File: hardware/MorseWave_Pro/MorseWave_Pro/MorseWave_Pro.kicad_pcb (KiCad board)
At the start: 2 copper layers, 85 x 65 mm, 33 parts, among them J1 PADDLE_3.5mm, J2 KEY_OUT_3.5mm, J3 PTT_OUT_RCA, J4 SPEAKER_8R, J5 OLED_0.96_I2C, J6 PS2_KEYBOARD, Q1 BC547, U2 PC817, U3 PC817

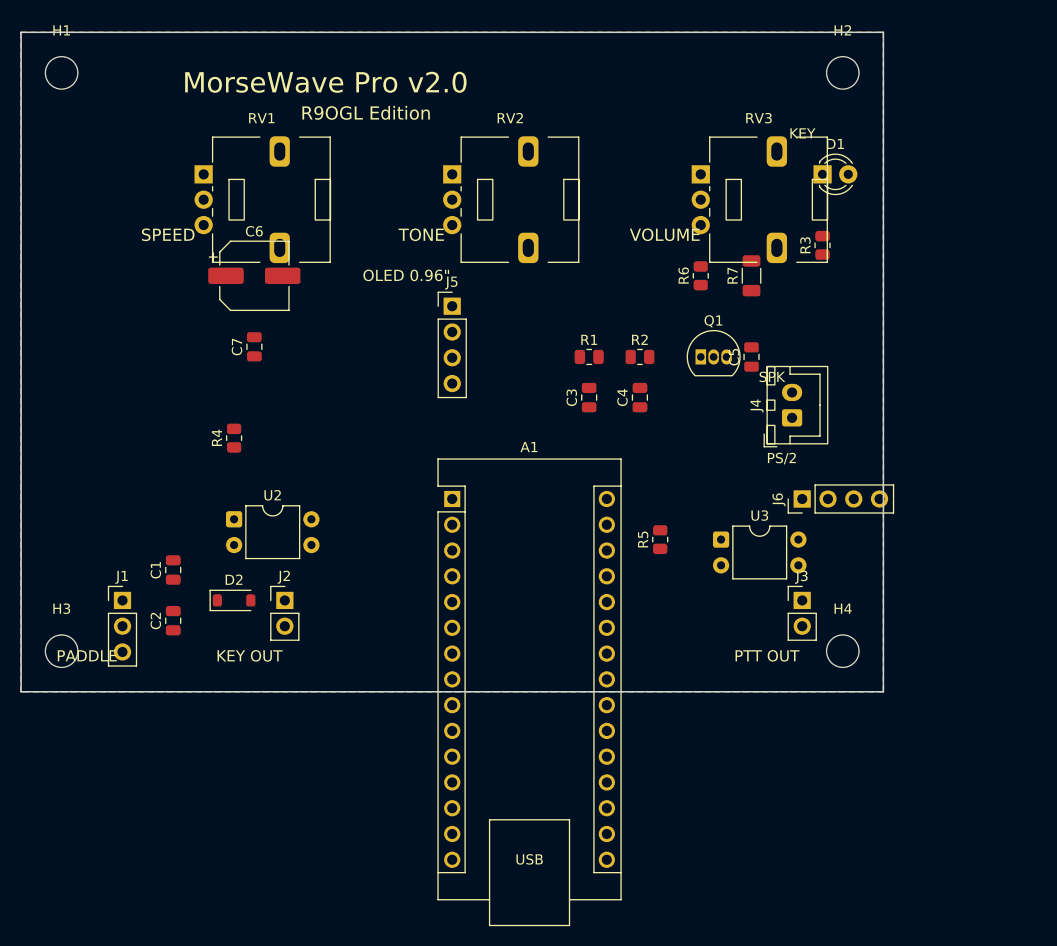
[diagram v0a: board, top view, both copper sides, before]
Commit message: Resize board to 100x75mm so Arduino Nano fits 100% inside with flush USB port
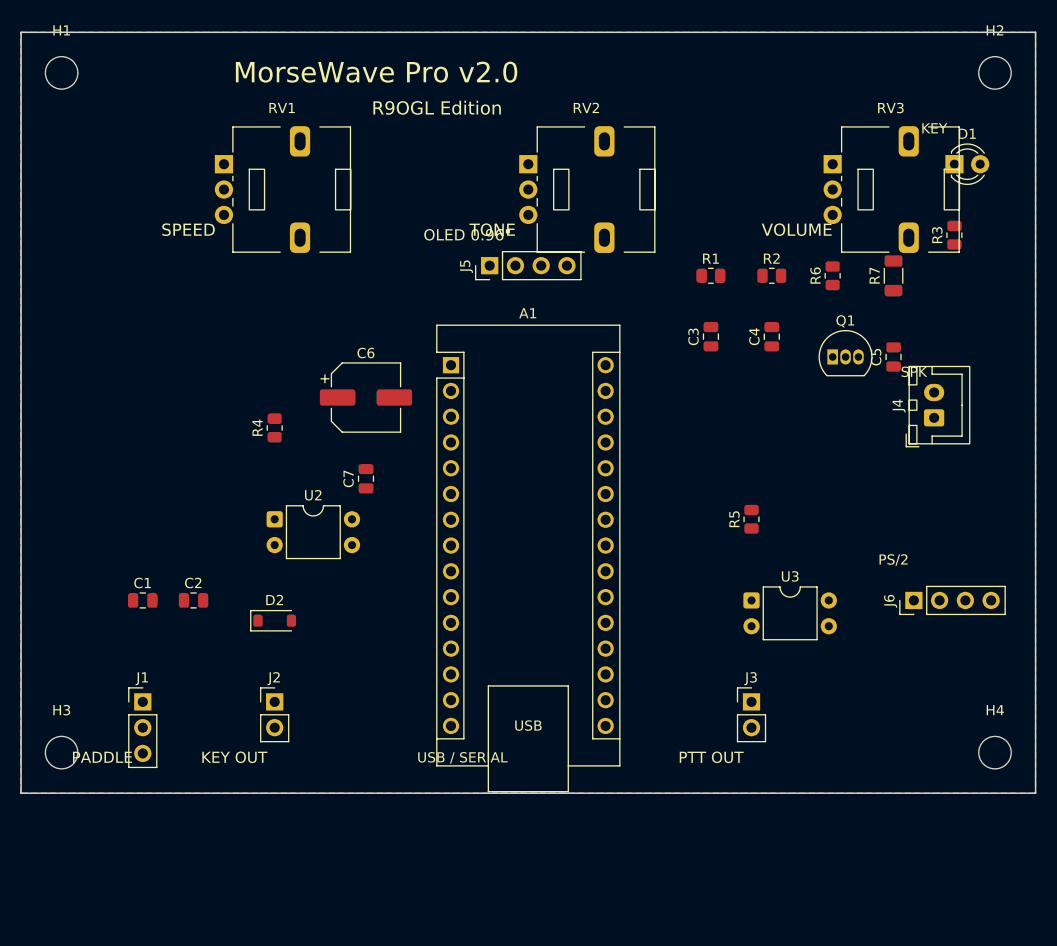
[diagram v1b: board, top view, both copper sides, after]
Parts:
- moved H4 18.0 mm to (96.0, 71.0)
- moved C7 17.0 mm to (34.0, 44.0)
- moved C6 16.3 mm to (34.0, 36.0)
- moved R2 15.3 mm to (74.0, 24.0)
- moved H2 15.0 mm to (96.0, 4.00)
- moved J6 14.9 mm to (88.0, 56.0)
- moved R1 14.4 mm to (68.0, 24.0)
- moved C4 14.3 mm to (74.0, 30.0)
- moved C5 14.0 mm to (86.0, 32.0)
- moved J4 14.0 mm to (90.0, 38.0)
- moved R7 14.0 mm to (86.0, 24.0)
- moved C3 13.4 mm to (68.0, 30.0)
- moved A1 13.2 mm to (42.4, 32.8)
- moved D1 13.0 mm to (92.0, 13.0)
- moved R3 13.0 mm to (92.0, 20.0)
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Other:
- board size 85 x 65 mm -> 100 x 75 mm
- board text added: "USB / SERIAL"

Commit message: feat(hardware): finalize 100% through-hole classic PCB v2.0 (100x75mm) and high-res 3D renders
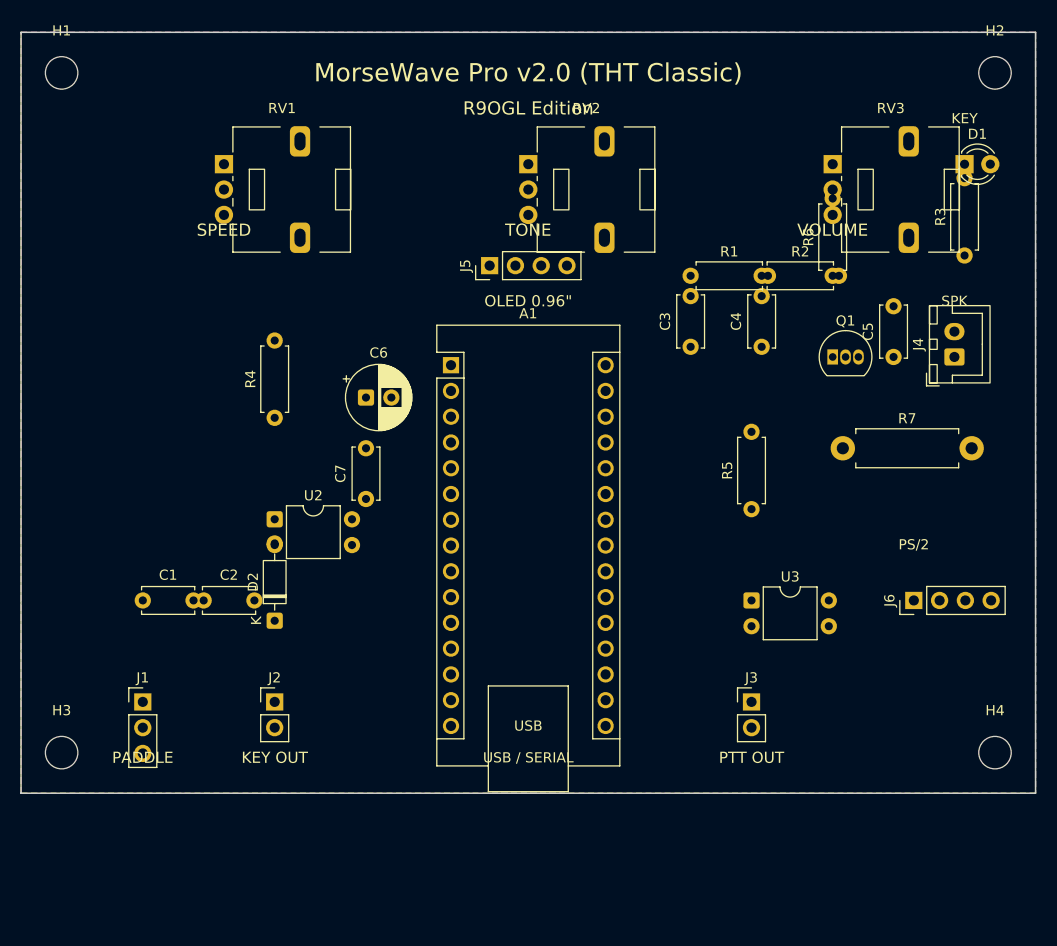
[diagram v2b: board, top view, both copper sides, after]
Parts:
- C1, C2, C3, C4, C5, C7: footprint C_0805_2012Metric -> C_Disc_D5.0mm_W2.5mm_P5.00mm
- C6: footprint CP_Elec_6.3x5.4 -> CP_Radial_D6.3mm_P2.50mm
- D2: footprint D_SOD-123 -> D_DO-35_SOD27_P7.62mm_Horizontal
- R1, R2, R3, R4, R5, R6: footprint R_0805_2012Metric -> R_Axial_DIN0207_L6.3mm_D2.5mm_P7.62mm_Horizontal
- R7: footprint R_1206_3216Metric -> R_Axial_DIN0411_L9.9mm_D3.6mm_P12.70mm_Horizontal
- moved R7 17.7 mm to (81.0, 41.0), turned to 0 degrees
- moved J4 6.32 mm to (92.0, 32.0)
- moved C3 2.24 mm to (66.0, 31.0)
- moved R3 2.24 mm to (93.0, 22.0)
- moved C7 2.00 mm to (34.0, 46.0)
- moved R1 2.00 mm to (66.0, 24.0)
- moved C4 1.41 mm to (73.0, 31.0)
- moved C2 1.00 mm to (18.0, 56.0)
- moved D1 1.00 mm to (93.0, 13.0)
- moved R2 1.00 mm to (73.0, 24.0)
- moved R4 1.00 mm to (25.0, 38.0)
- moved R5 1.00 mm to (72.0, 47.0)
- turned D2 to 90 degrees
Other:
- board text added: "MorseWave Pro v2.0 (THT Classic)"
- board text removed: "MorseWave Pro v2.0"

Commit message: feat(hardware): clean silkscreen overlaps, add telegraph key logo, By R9OGL, website, and Rezonit fab compliance
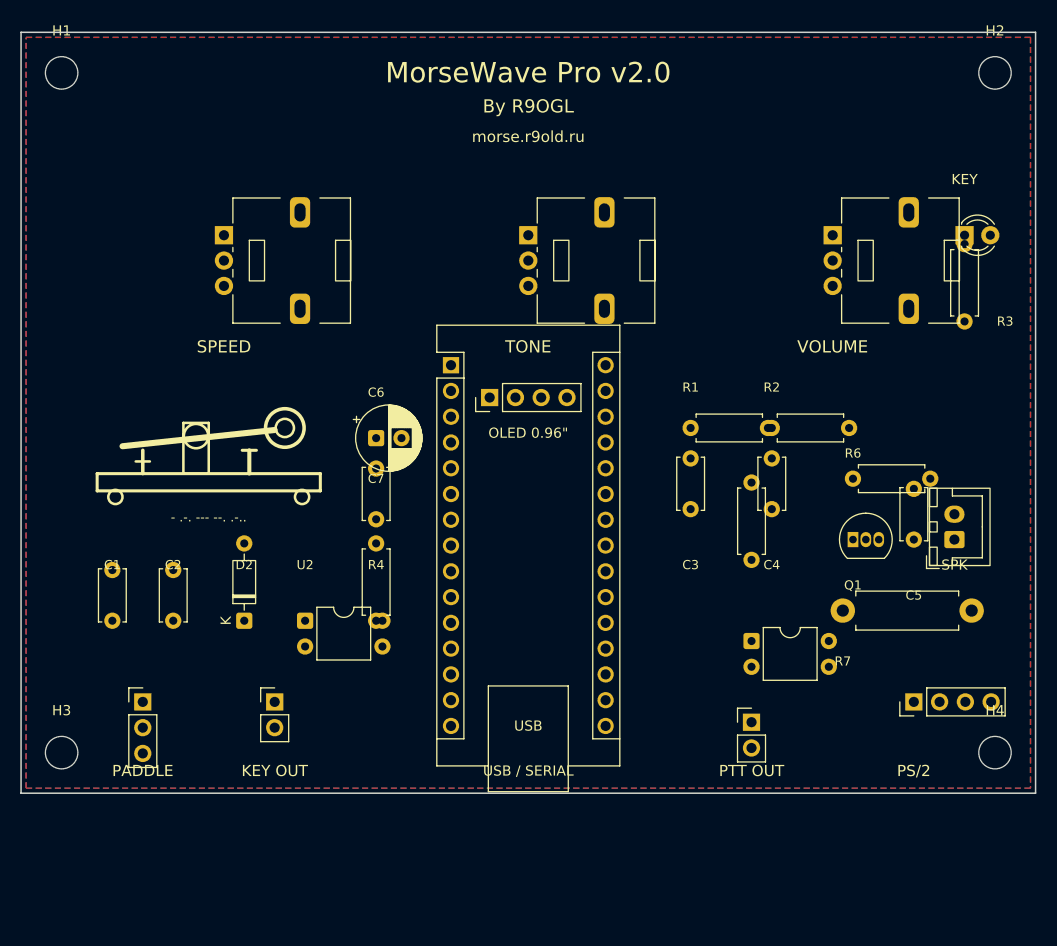
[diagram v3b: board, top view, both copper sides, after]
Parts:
- moved R4 22.4 mm to (35.0, 58.0)
- moved R6 20.1 mm to (82.0, 44.0), turned to 0 degrees
- moved C5 18.1 mm to (88.0, 50.0)
- moved Q1 18.1 mm to (82.0, 50.0)
- moved J4 18.0 mm to (92.0, 50.0)
- moved C4 16.0 mm to (74.0, 47.0)
- moved C3 16.0 mm to (66.0, 47.0)
- moved R7 16.0 mm to (81.0, 57.0)
- moved R2 15.0 mm to (74.0, 39.0)
- moved R1 15.0 mm to (66.0, 39.0)
- moved J5 13.0 mm to (46.2, 36.0)
- moved U2 10.4 mm to (28.0, 58.0)
- moved J6 10.0 mm to (88.0, 66.0)
- moved D1 7.00 mm to (93.0, 20.0)
- moved RV1 7.00 mm to (20.0, 20.0)
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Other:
- rule pad_to_mask_clearance: 0 -> 0.05
- board text added: "- .-. --- --. .-.."
- board text added: "By R9OGL"
- board text added: "C1"
- board text added: "C2"
- board text added: "C3"
- board text added: "C4"
- board text added: "C5"
- board text added: "C6"
- board text added: "C7"
- board text added: "D2"
- board text added: "MorseWave Pro v2.0"
- board text added: "Q1"
- board text added: "R1"
- board text added: "R2"
- board text added: "R3"
- board text added: "R4"
- board text added: "R6"
- board text added: "R7"
- board text added: "U2"
- board text added: "morse.r9old.ru"
- board text removed: "MorseWave Pro v2.0 (THT Classic)"
- board text removed: "R9OGL Edition"

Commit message: feat(hardware): finalize MorseWave Pro v2.0 THT PCB with 0 DRC errors, dedicated OLED zone, and Rezonit Gerbers
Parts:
- added J7: PHONES_3.5mm, PinHeader_1x02_P2.54mm_Vertical, F.Cu at (89.6, 67.0)
- added J_LED: TX_LED_WIRES, PinHeader_1x02_P2.54mm_Vertical, F.Cu at (93.0, 20.0)
- added J_RV1: SPEED_WIRES, PinHeader_1x03_P2.54mm_Vertical, F.Cu at (30.0, 13.5)
- added J_RV2: TONE_WIRES, PinHeader_1x03_P2.54mm_Vertical, F.Cu at (58.0, 13.5)
- added J_RV3: VOL_WIRES, PinHeader_1x03_P2.54mm_Vertical, F.Cu at (85.0, 13.5)
- added R8: 150R, R_Axial_DIN0207_L6.3mm_D2.5mm_P7.62mm_Horizontal, F.Cu at (82.0, 62.0)
- D1: value LED_KEY -> TX_GREEN_3mm
- moved J5 27.6 mm to (19.0, 31.0)
- moved C6 25.1 mm to (10.0, 38.0)
- moved C7 19.7 mm to (18.0, 38.0), turned to 0 degrees
- moved R6 16.5 mm to (66.0, 48.0)
- moved R7 15.3 mm to (66.0, 54.0)
- moved D2 14.1 mm to (36.0, 56.0), turned to -90 degrees
- moved RV3 13.6 mm to (68.0, 13.5)
- moved R4 13.6 mm to (24.0, 50.0), turned to 0 degrees
- moved R5 12.7 mm to (63.0, 61.0), turned to 0 degrees
- moved J6 12.2 mm to (95.0, 56.0), turned to 0 degrees
- moved J4 12.2 mm to (94.0, 38.0), turned to 0 degrees
- moved RV2 11.1 mm to (41.0, 13.5)
- moved J2 11.0 mm to (36.0, 67.0)
- moved RV1 8.85 mm to (14.0, 13.5)
- moved J3 8.06 mm to (80.0, 67.0)
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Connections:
- A1 pad 11: unconnected-(A1-D8-Pad11) -> /LED_KEY
- A1 pad 12: /AUDIO_PWM -> unconnected-(A1-D9-Pad12)
- A1 pad 16: /LED_KEY -> unconnected-(A1-D13-Pad16)
- A1 pad 20: /POT_TONE -> unconnected-(A1-A1-Pad20)
- A1 pad 21: unconnected-(A1-A2-Pad21) -> /POT_TONE
- A1 pad 9: unconnected-(A1-D6-Pad9) -> /AUDIO_PWM
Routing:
- net +5V: track 0.00 -> 293.7 mm, vias 0 -> 2
- net /PS2_DATA: track 0.00 -> 100.1 mm, vias 0 -> 1
- net /POT_SPEED: track 0.00 -> 99.3 mm
- net /PS2_CLK: track 0.00 -> 91.0 mm, vias 0 -> 2
- net /LED_KEY: track 0.00 -> 82.5 mm, vias 0 -> 1
- net /DIT: track 0.00 -> 71.2 mm
- net /POT_TONE: track 0.00 -> 65.2 mm, vias 0 -> 1
- net /AUDIO_PWM: track 0.00 -> 59.9 mm, vias 0 -> 1
- net /DAH: track 0.00 -> 59.2 mm
- net Net-(J_RV3-Pin_1): track 0.00 -> 56.7 mm
- net /OLED_SDA: track 0.00 -> 55.9 mm
- net /OLED_SCL: track 0.00 -> 55.8 mm, vias 0 -> 1
- net Net-(J_RV3-Pin_2): track 0.00 -> 55.0 mm, vias 0 -> 1
- net Net-(J4-Pin_1): track 0.00 -> 52.0 mm
- net Net-(J4-Pin_2): track 0.00 -> 46.5 mm
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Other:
- board text added: "-.. . .-. ----. --- --. .-.."
- board text added: "3V3"
- board text added: "5V"
- board text added: "A0"
- board text added: "A1"
- board text added: "A2"
- board text added: "A3"
- board text added: "A4"
- board text added: "A5"
- board text added: "A6"
- board text added: "A7"
- board text added: "D10"
- board text added: "D11"
- board text added: "D12"
- board text added: "D13"
- board text added: "D3"
- board text added: "D4"
- board text added: "D5"
- board text added: "D6"
- board text added: "D7"
- board text added: "D8"
- board text added: "D9"
- board text added: "GND"
- board text added: "GND VCC SCL SDA"
- board text added: "MorseWave Pro v2.0 * DE R9OGL"
- board text added: "OLED 0.96" I2C"
- board text added: "PHONES"
- board text added: "R5"
- board text added: "R8"
- board text added: "REF"
- board text added: "RST"
- board text added: "RX"
- board text added: "TX"
- board text added: "TX (GREEN)"
- board text added: "U3"
- board text added: "USB SERIAL"
- board text added: "VIN"
- board text added: "Website: morse.r9old.ru"
- board text removed: "- .-. --- --. .-.."
- board text removed: "By R9OGL"
- board text removed: "KEY"
- board text removed: "MorseWave Pro v2.0"
- board text removed: "OLED 0.96""
- board text removed: "USB / SERIAL"
- board text removed: "morse.r9old.ru"
